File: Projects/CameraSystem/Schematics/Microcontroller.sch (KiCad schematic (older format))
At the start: 25 parts, among them J2 Conn_02x03_Odd_Even, J3 Conn_01x02, J4 Conn_01x03, J5 Conn_01x02, U3 ATMEGA16A-AU, Y2 ABLS2-10.000MHZ-D4Y-T

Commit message: replace tvs diodes of camera system
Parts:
- removed C10: 100n, digikey-footprints:0603, symbol Device:C
- removed D5: BZX84C3V3LT1G, custom-footprints:SOT−23_(TO−236), symbol Device:D_Zener
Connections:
- net labels added: U2_SPI_RST, UC_SPI_RX, UC_SPI_TX
- net labels removed: SPI_RST
- wire segments 135 -> 128
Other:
- moved on the sheet: R8, R9, S1
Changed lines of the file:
@@
 Comment4 ""
 $EndDescr
-Text HLabel 1650 800  0    60   Input ~ 0
+Text HLabel 1900 800  0    60   Input ~ 0
 VDD_3V3
-Text HLabel 1650 1700 0    60   Input ~ 0
-SPI_RST
+Text HLabel 1900 1700 0    60   Input ~ 0
+U2_SPI_RST
 Text HLabel 6650 4500 2    60   Output ~ 0
-SPI_TX
+UC_SPI_TX
 Text HLabel 6650 4400 2    60   Input ~ 0
-SPI_RX
+UC_SPI_RX
 $Comp
 L CameraSystem-rescue:ATMEGA16A-AU U?
@@
 L Device:R R8
 U 1 1 5BB8AD84
-P 2000 1200
-F 0 "R8" V 2080 1200 50  0000 C CNN
-F 1 "10k" V 2000 1200 50  0000 C CNN
-F 2 "digikey-footprints:0603" V 1930 1200 50  0001 C CNN
-F 3 "" H 2000 1200 50  0001 C CNN
-	1    2000 1200
-	1    0    0    -1
-$EndComp
-$Comp
-L Device:D_Zener D5
-U 1 1 5BB8ADE9
-P 3000 1200
-F 0 "D5" H 3000 1300 50  0000 C CNN
-F 1 "BZX84C3V3LT1G" H 3000 1100 50  0000 C CNN
-F 2 "custom-footprints:SOT−23_(TO−236)" H 3000 1400 50  0001 C CNN
-F 3 "" H 3000 1200 50  0001 C CNN
-	1    3000 1200
-	0    1    1    0
+P 2250 1200
+F 0 "R8" V 2330 1200 50  0000 C CNN
+F 1 "10k" V 2250 1200 50  0000 C CNN
+F 2 "digikey-footprints:0603" V 2180 1200 50  0001 C CNN
+F 3 "" H 2250 1200 50  0001 C CNN
+	1    2250 1200
+	1    0    0    -1
 $EndComp
 $Comp
 L power:GND #PWR0109
 U 1 1 5BB8B0A7
-P 2000 3100
-F 0 "#PWR0109" H 2000 2850 50  0001 C CNN
-F 1 "GND" H 2000 2950 50  0000 C CNN
-F 2 "" H 2000 3100 50  0001 C CNN
-F 3 "" H 2000 3100 50  0001 C CNN
-	1    2000 3100
+P 2250 3100
+F 0 "#PWR0109" H 2250 2850 50  0001 C CNN
+F 1 "GND" H 2250 2950 50  0000 C CNN
+F 2 "" H 2250 3100 50  0001 C CNN
+F 3 "" H 2250 3100 50  0001 C CNN
+	1    2250 3100
 	1    0    0    -1
 $EndComp
@@
 L Device:R R9
 U 1 1 5BB8C561
-P 2000 2050
-F 0 "R9" V 2080 2050 50  0000 C CNN
-F 1 "330" V 2000 2050 50  0000 C CNN
-F 2 "digikey-footprints:0603" V 1930 2050 50  0001 C CNN
-F 3 "" H 2000 2050 50  0001 C CNN
-	1    2000 2050
+P 2250 2050
+F 0 "R9" V 2330 2050 50  0000 C CNN
+F 1 "330" V 2250 2050 50  0000 C CNN
+F 2 "digikey-footprints:0603" V 2180 2050 50  0001 C CNN
+F 3 "" H 2250 2050 50  0001 C CNN
+	1    2250 2050
 	1    0    0    -1
 $EndComp
@@
 L CameraSystem-rescue:KS-01Q-01 S?
 U 1 1 5BB8C7F1
-P 2000 2650
+P 2250 2650
 AR Path="/5BB8C7F1" Ref="S?"  Part="1"
 AR Path="/5BB4D99F/5BB8C7F1" Ref="S1"  Part="1"
-F 0 "S1" H 2000 2850 50  0000 C CNN
-F 1 "KS-01Q-01" H 2000 2475 50  0000 C CNN
-F 2 "digikey-footprints:PushButton_Round_D12mm_THT_KS-01Q-01" H 2200 2850 50  0001 L CNN
-F 3 "http://spec_sheets.e-switch.com/specs/29-KS01Q01.pdf" H 2200 2950 60  0001 L CNN
-F 4 "EG4791-ND" H 2200 3050 60  0001 L CNN "Digi-Key_PN"
-F 5 "KS-01Q-01" H 2200 3150 60  0001 L CNN "MPN"
-F 6 "Switches" H 2200 3250 60  0001 L CNN "Category"
-F 7 "Pushbutton Switches" H 2200 3350 60  0001 L CNN "Family"
-F 8 "http://spec_sheets.e-switch.com/specs/29-KS01Q01.pdf" H 2200 3450 60  0001 L CNN "DK_Datasheet_Link"
-F 9 "/product-detail/en/e-switch/KS-01Q-01/EG4791-ND/2116270" H 2200 3550 60  0001 L CNN "DK_Detail_Page"
-F 10 "SWITCH PUSH SPST-NO 0.01A 35V" H 2200 3650 60  0001 L CNN "Description"
-F 11 "E-Switch" H 2200 3750 60  0001 L CNN "Manufacturer"
-F 12 "Active" H 2200 3850 60  0001 L CNN "Status"
-	1    2000 2650
+F 0 "S1" H 2250 2850 50  0000 C CNN
+F 1 "KS-01Q-01" H 2250 2475 50  0000 C CNN
+F 2 "digikey-footprints:PushButton_Round_D12mm_THT_KS-01Q-01" H 2450 2850 50  0001 L CNN
+F 3 "http://spec_sheets.e-switch.com/specs/29-KS01Q01.pdf" H 2450 2950 60  0001 L CNN
+F 4 "EG4791-ND" H 2450 3050 60  0001 L CNN "Digi-Key_PN"
+F 5 "KS-01Q-01" H 2450 3150 60  0001 L CNN "MPN"
+F 6 "Switches" H 2450 3250 60  0001 L CNN "Category"
+F 7 "Pushbutton Switches" H 2450 3350 60  0001 L CNN "Family"
+F 8 "http://spec_sheets.e-switch.com/specs/29-KS01Q01.pdf" H 2450 3450 60  0001 L CNN "DK_Datasheet_Link"
+F 9 "/product-detail/en/e-switch/KS-01Q-01/EG4791-ND/2116270" H 2450 3550 60  0001 L CNN "DK_Detail_Page"
+F 10 "SWITCH PUSH SPST-NO 0.01A 35V" H 2450 3650 60  0001 L CNN "Description"
+F 11 "E-Switch" H 2450 3750 60  0001 L CNN "Manufacturer"
+F 12 "Active" H 2450 3850 60  0001 L CNN "Status"
+	1    2250 2650
 	0    -1   -1   0
 $EndComp
@@
 	6350 4400 6650 4400
 Wire Wire Line
-	1650 1700 2000 1700
-Wire Wire Line
-	2000 1700 2400 1700
-Wire Wire Line
-	2400 1700 3000 1700
-Wire Wire Line
-	3000 1700 4150 1700
-Wire Wire Line
-	1650 800  2000 800
-Wire Wire Line
-	2000 800  3000 800
-Wire Wire Line
-	3000 800  4050 800
+	1900 1700 2250 1700
+Wire Wire Line
+	1900 800  2250 800
 Wire Wire Line
 	4050 800  4350 800
@@
 Connection ~ 5050 5500
 Wire Wire Line
-	2000 800  2000 1050
-Connection ~ 2000 800
-Wire Wire Line
-	2000 1350 2000 1700
-Wire Wire Line
-	2000 1700 2000 1900
-Connection ~ 2000 1700
-Wire Wire Line
-	3000 1050 3000 800
-Connection ~ 3000 800
-Wire Wire Line
-	3000 1350 3000 1700
-Connection ~ 3000 1700
+	2250 800  2250 1050
+Connection ~ 2250 800
+Wire Wire Line
+	2250 1350 2250 1700
+Wire Wire Line
+	2250 1700 2250 1900
+Connection ~ 2250 1700
 Wire Wire Line
 	2950 3500 2950 3400
@@
 	4050 1200 4050 1250
 Wire Wire Line
-	1900 2450 1900 2400
-Wire Wire Line
-	1900 2400 2000 2400
-Wire Wire Line
-	2000 2400 2100 2400
-Wire Wire Line
-	2100 2400 2100 2450
-Wire Wire Line
-	1900 2850 1900 2900
-Wire Wire Line
-	1900 2900 2000 2900
-Wire Wire Line
-	2000 2900 2100 2900
-Wire Wire Line
-	2100 2900 2100 2850
-Wire Wire Line
-	2000 2200 2000 2400
-Connection ~ 2000 2400
-Wire Wire Line
-	2000 2900 2000 3100
-Connection ~ 2000 2900
+	2150 2450 2150 2400
+Wire Wire Line
+	2150 2400 2250 2400
+Wire Wire Line
+	2250 2400 2350 2400
+Wire Wire Line
+	2350 2400 2350 2450
+Wire Wire Line
+	2150 2850 2150 2900
+Wire Wire Line
+	2150 2900 2250 2900
+Wire Wire Line
+	2250 2900 2350 2900
+Wire Wire Line
+	2350 2900 2350 2850
+Wire Wire Line
+	2250 2200 2250 2400
+Connection ~ 2250 2400
+Wire Wire Line
+	2250 2900 2250 3100
+Connection ~ 2250 2900
 Wire Wire Line
 	1700 4850 1600 4850
@@
 Text HLabel 6650 5000 2    60   Output ~ 0
 CAM_XCLK_CTL
-$Comp
-L Device:C C10
-U 1 1 5BBE76EA
-P 2400 2700
-F 0 "C10" H 2425 2800 50  0000 L CNN
-F 1 "100n" H 2425 2600 50  0000 L CNN
-F 2 "digikey-footprints:0603" H 2438 2550 50  0001 C CNN
-F 3 "" H 2400 2700 50  0001 C CNN
-	1    2400 2700
-	1    0    0    -1
-$EndComp
-Wire Wire Line
-	2400 2550 2400 1700
-Connection ~ 2400 1700
-Wire Wire Line
-	2400 2850 2400 3100
-$Comp
-L power:GND #PWR0118
-U 1 1 5BBE788F
-P 2400 3100
-F 0 "#PWR0118" H 2400 2850 50  0001 C CNN
-F 1 "GND" H 2400 2950 50  0000 C CNN
-F 2 "" H 2400 3100 50  0001 C CNN
-F 3 "" H 2400 3100 50  0001 C CNN
-	1    2400 3100
-	1    0    0    -1
-$EndComp
 Wire Wire Line
 	6350 3700 6950 3700
@@
 Wire Wire Line
 	2200 4950 2850 4950
+Wire Wire Line
+	2250 1700 4150 1700
+Wire Wire Line
+	2250 800  4050 800
 $EndSCHEMATC

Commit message: linux adaptation
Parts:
- added D?: SMBJ5.0CA, symbol Device:D_TVS
- D6: value APG1608SYKC/T -> LED; footprint custom-footprints:LED_APG1608 -> LED_SMD:LED_1206_3216Metric
- S1: value KS-01Q-01 -> S; footprint digikey-footprints:PushButton_Round_D12mm_THT_KS-01Q-01 -> (none); Category Switches -> (none); DK_Datasheet_Link http://spec_sheets.e-switch.com/specs/29-KS01Q01.pdf -> (none); DK_Detail_Page /product-detail/en/e-switch/KS-01Q-01/EG4791-ND/2116270 -> (none); Description SWITCH PUSH SPST-NO 0.01A 35V -> (none); Digi-Key_PN EG4791-ND -> (none); Family Pushbutton Switches -> (none); MPN KS-01Q-01 -> (none); Manufacturer E-Switch -> (none); Status Active -> (none)
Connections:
- net U2_SPI_RST: now also D?.2 (A2)
- net VDD_3V3: now also D?.1 (A1)
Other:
- note added: "i2c pull up resistors might be adapted in order to match the level shifter"
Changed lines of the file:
@@
 AR Path="/5BB4D99F/5BB8C7F1" Ref="S1"  Part="1"
 F 0 "S1" H 2250 2850 50  0000 C CNN
-F 1 "KS-01Q-01" H 2250 2475 50  0000 C CNN
-F 2 "digikey-footprints:PushButton_Round_D12mm_THT_KS-01Q-01" H 2450 2850 50  0001 L CNN
-F 3 "http://spec_sheets.e-switch.com/specs/29-KS01Q01.pdf" H 2450 2950 60  0001 L CNN
-F 4 "EG4791-ND" H 2450 3050 60  0001 L CNN "Digi-Key_PN"
-F 5 "KS-01Q-01" H 2450 3150 60  0001 L CNN "MPN"
-F 6 "Switches" H 2450 3250 60  0001 L CNN "Category"
-F 7 "Pushbutton Switches" H 2450 3350 60  0001 L CNN "Family"
-F 8 "http://spec_sheets.e-switch.com/specs/29-KS01Q01.pdf" H 2450 3450 60  0001 L CNN "DK_Datasheet_Link"
-F 9 "/product-detail/en/e-switch/KS-01Q-01/EG4791-ND/2116270" H 2450 3550 60  0001 L CNN "DK_Detail_Page"
-F 10 "SWITCH PUSH SPST-NO 0.01A 35V" H 2450 3650 60  0001 L CNN "Description"
-F 11 "E-Switch" H 2450 3750 60  0001 L CNN "Manufacturer"
-F 12 "Active" H 2450 3850 60  0001 L CNN "Status"
+F 1 "S" H 2250 2475 50  0000 C CNN
+F 2 "" H 2450 2850 50  0001 L CNN
+F 3 "" H 2450 2950 60  0001 L CNN
 	1    2250 2650
 	0    -1   -1   0
@@
 SDA_3V3
 $Comp
-L Device:LED D6
-U 1 1 5BBA7F65
-P 8400 4000
-F 0 "D6" H 8400 4100 50  0000 C CNN
-F 1 "APG1608SYKC/T" H 8400 3900 50  0000 C CNN
-F 2 "custom-footprints:LED_APG1608" H 8400 4000 50  0001 C CNN
-F 3 "" H 8400 4000 50  0001 C CNN
-	1    8400 4000
-	0    -1   -1   0
-$EndComp
-$Comp
 L Device:R R21
 U 1 1 5BBA823A
@@
 	2200 4950 2850 4950
 Wire Wire Line
-	2250 1700 4150 1700
-Wire Wire Line
-	2250 800  4050 800
+	2250 1700 2900 1700
+Wire Wire Line
+	2250 800  2900 800
+$Comp
+L Device:LED D6
+U 1 1 5CA538DC
+P 8400 4000
+F 0 "D6" V 8438 3883 50  0000 R CNN
+F 1 "LED" V 8347 3883 50  0000 R CNN
+F 2 "LED_SMD:LED_1206_3216Metric" H 8400 4000 50  0001 C CNN
+F 3 "~" H 8400 4000 50  0001 C CNN
+	1    8400 4000
+	0    -1   -1   0
+$EndComp
+$Comp
+L Device:D_TVS D?
+U 1 1 5CA48BC2
+P 2900 1200
+F 0 "D?" V 2854 1279 50  0000 L CNN
+F 1 "SMBJ5.0CA" V 2945 1279 50  0000 L CNN
+F 2 "" H 2900 1200 50  0001 C CNN
+F 3 "~" H 2900 1200 50  0001 C CNN
+	1    2900 1200
+	0    1    1    0
+$EndComp
+Wire Wire Line
+	2900 1050 2900 800
+Connection ~ 2900 800
+Wire Wire Line
+	2900 800  4050 800
+Wire Wire Line
+	2900 1350 2900 1700
+Connection ~ 2900 1700
+Wire Wire Line
+	2900 1700 4150 1700
+Text Notes 7850 2750 0    50   ~ 0
+i2c pull up resistors might be adapted in order to match the level shifter
 $EndSCHEMATC

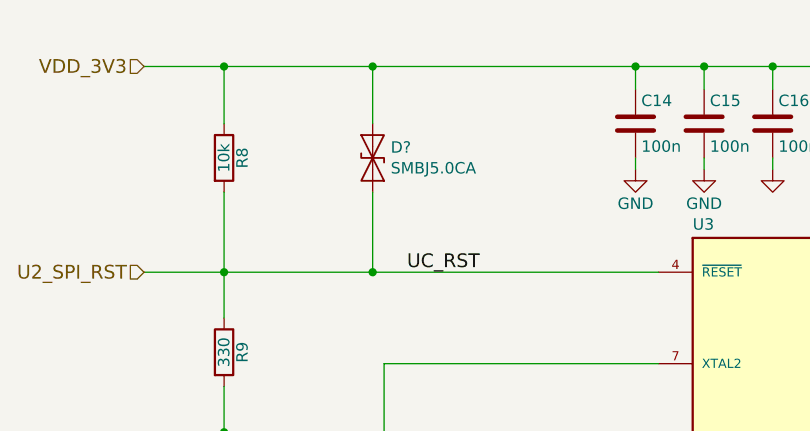
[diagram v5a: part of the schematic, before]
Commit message: wifi module added
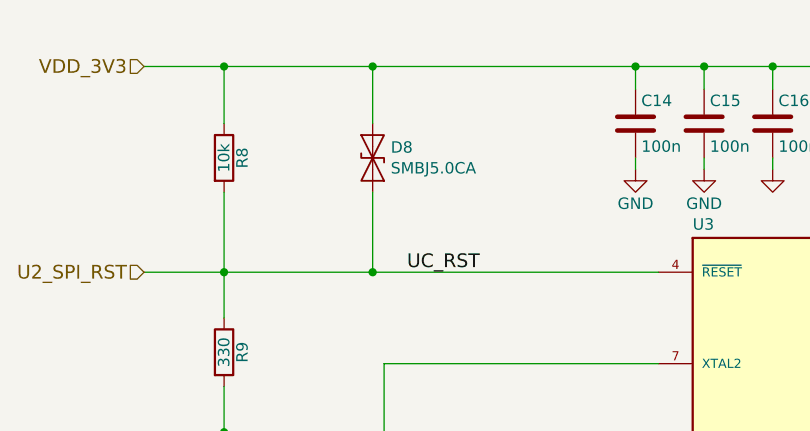
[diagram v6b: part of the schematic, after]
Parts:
- gave numbers to parts that had none: 1
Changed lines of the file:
@@
 $EndComp
 $Comp
-L Device:D_TVS D?
+L Device:D_TVS D8
 U 1 1 5CA48BC2
 P 2900 1200
-F 0 "D?" V 2854 1279 50  0000 L CNN
+F 0 "D8" V 2854 1279 50  0000 L CNN
 F 1 "SMBJ5.0CA" V 2945 1279 50  0000 L CNN
 F 2 "" H 2900 1200 50  0001 C CNN

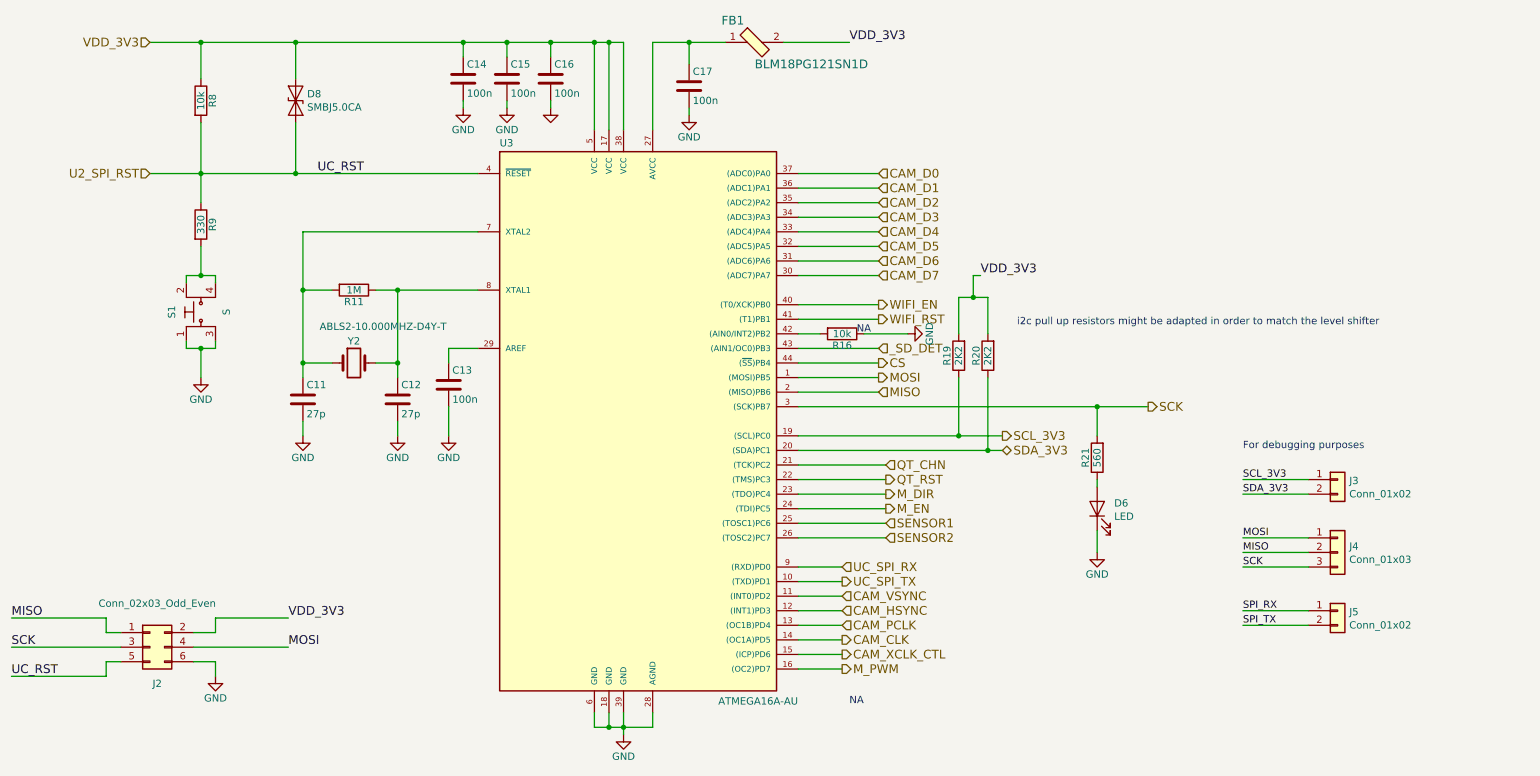
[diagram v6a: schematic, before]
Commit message: camera was updated
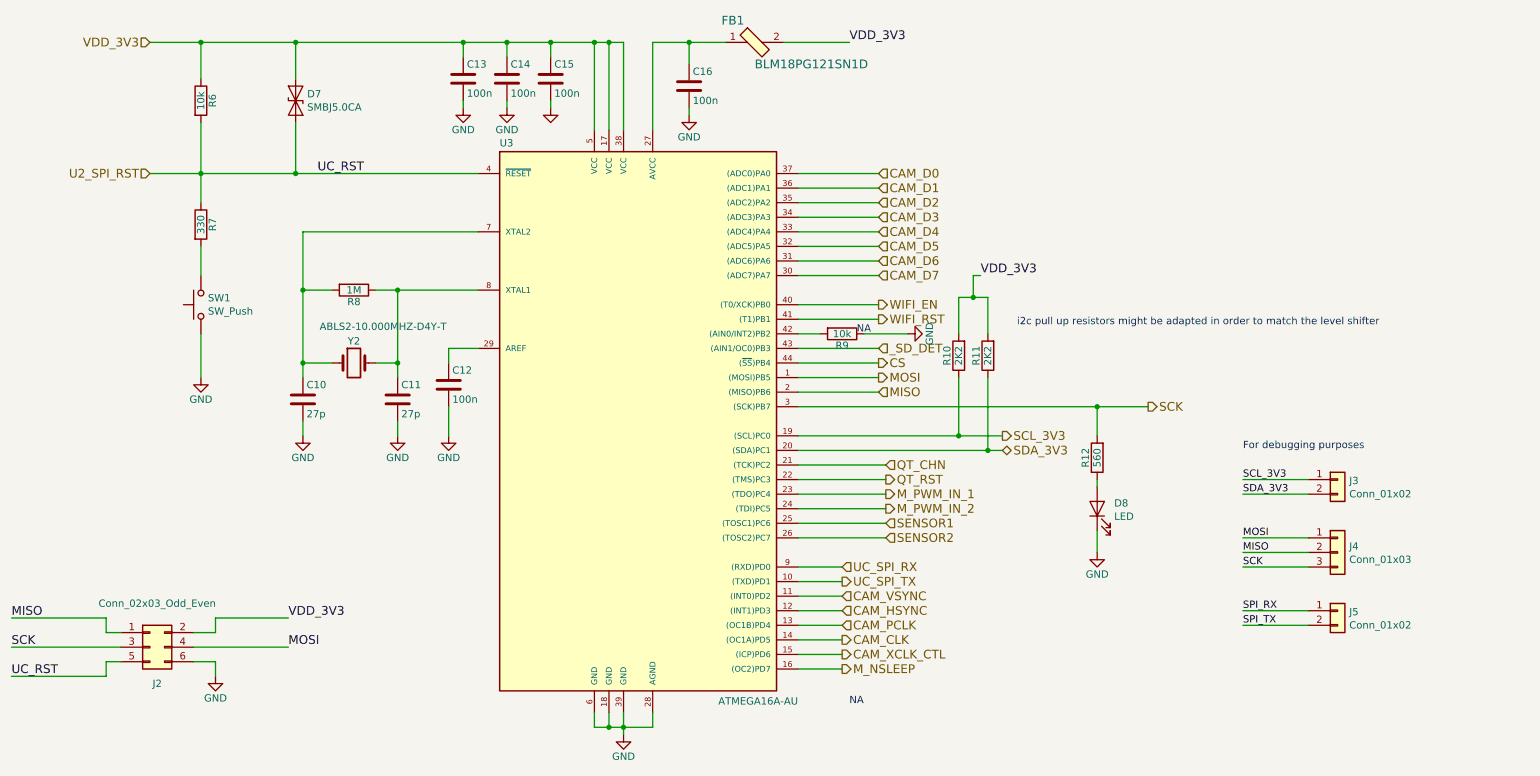
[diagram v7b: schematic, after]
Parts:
- removed S1: S, symbol CameraSystem-rescue:KS-01Q-01
- added SW1: SW_Push, Button_Switch_THT:SW_PUSH_6mm_H4.3mm, symbol Switch:SW_Push
- C10: renamed from C11; footprint digikey-footprints:0603 -> Capacitor_SMD:C_0603_1608Metric_Pad1.05x0.95mm_HandSolder
- C11: renamed from C12; footprint digikey-footprints:0603 -> Capacitor_SMD:C_0603_1608Metric_Pad1.05x0.95mm_HandSolder
- C12: renamed from C13; footprint digikey-footprints:0603 -> Capacitor_SMD:C_0603_1608Metric_Pad1.05x0.95mm_HandSolder
- C13: renamed from C14; footprint digikey-footprints:0603 -> Capacitor_SMD:C_0603_1608Metric_Pad1.05x0.95mm_HandSolder
- C14: renamed from C15; footprint digikey-footprints:0603 -> Capacitor_SMD:C_0603_1608Metric_Pad1.05x0.95mm_HandSolder
- C15: renamed from C16; footprint digikey-footprints:0603 -> Capacitor_SMD:C_0603_1608Metric_Pad1.05x0.95mm_HandSolder
- C16: renamed from C17; footprint digikey-footprints:0603 -> Capacitor_SMD:C_0603_1608Metric_Pad1.05x0.95mm_HandSolder
- D7: renamed from D8; footprint (none) -> custom-footprints:SMB_DO-214AA
- FB1: footprint digikey-footprints:0603 -> Resistor_SMD:R_0603_1608Metric_Pad1.05x0.95mm_HandSolder
- J2: footprint Pin_Headers:Pin_Header_Straight_2x03_Pitch2.54mm -> Connector_PinSocket_2.54mm:PinSocket_2x03_P2.54mm_Vertical
- J3, J5: footprint Pin_Headers:Pin_Header_Straight_1x02_Pitch2.54mm -> Connector_PinSocket_2.54mm:PinSocket_1x02_P2.54mm_Vertical
- J4: footprint Pin_Headers:Pin_Header_Straight_1x03_Pitch2.54mm -> Connector_PinSocket_2.54mm:PinSocket_1x03_P2.54mm_Horizontal
- R10: renamed from R19; footprint digikey-footprints:0603 -> Resistor_SMD:R_0603_1608Metric_Pad1.05x0.95mm_HandSolder
- R11: renamed from R20; footprint digikey-footprints:0603 -> Resistor_SMD:R_0603_1608Metric_Pad1.05x0.95mm_HandSolder
- R12: renamed from R21; footprint digikey-footprints:0603 -> Resistor_SMD:R_0603_1608Metric_Pad1.05x0.95mm_HandSolder
- R6: renamed from R8; footprint digikey-footprints:0603 -> Resistor_SMD:R_0603_1608Metric_Pad1.05x0.95mm_HandSolder
- R7: renamed from R9; footprint digikey-footprints:0603 -> Resistor_SMD:R_0603_1608Metric_Pad1.05x0.95mm_HandSolder
- R8: renamed from R11; footprint digikey-footprints:0603 -> Resistor_SMD:R_0603_1608Metric_Pad1.05x0.95mm_HandSolder
- R9: renamed from R16; footprint digikey-footprints:0603 -> Resistor_SMD:R_0603_1608Metric_Pad1.05x0.95mm_HandSolder
- renumbered D6 to D8
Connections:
- net GND: now also SW1.1
- net at R7.2: now also SW1.2
- net M_DIR renamed M_PWM_IN_1
- net M_EN renamed M_PWM_IN_2
- net M_PWM renamed M_NSLEEP
